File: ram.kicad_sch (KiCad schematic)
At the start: 8 parts, among them U8 HyperRAM

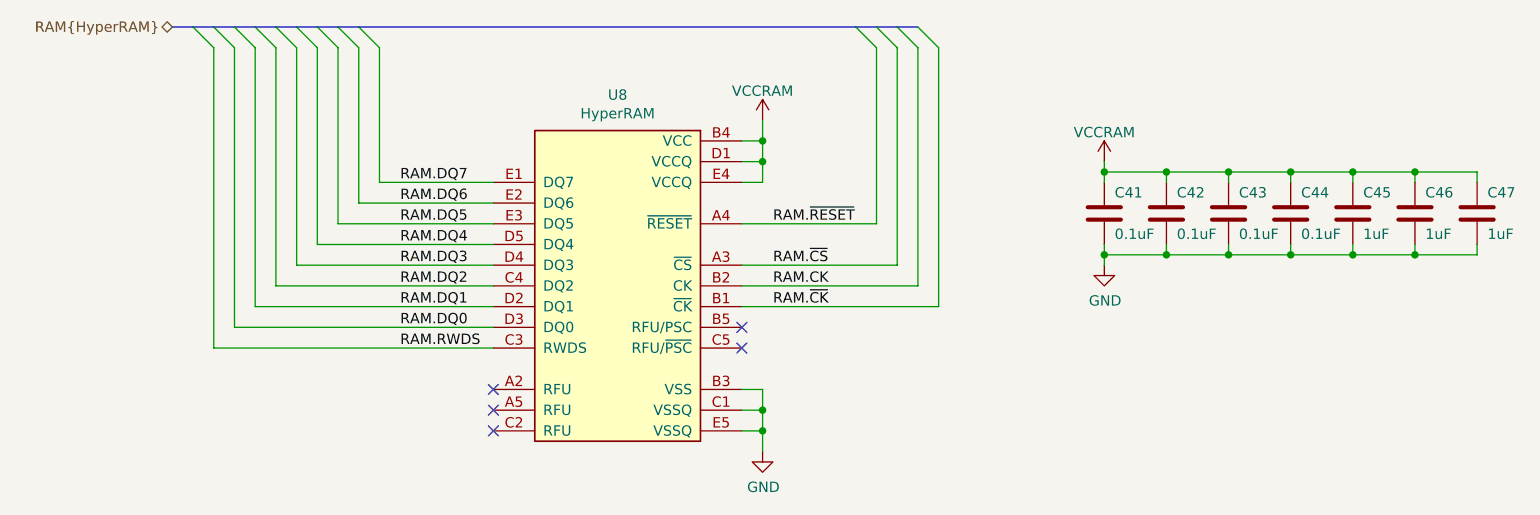
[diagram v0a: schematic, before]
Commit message: Add radio transceiver
Remove Cynthion-specific features
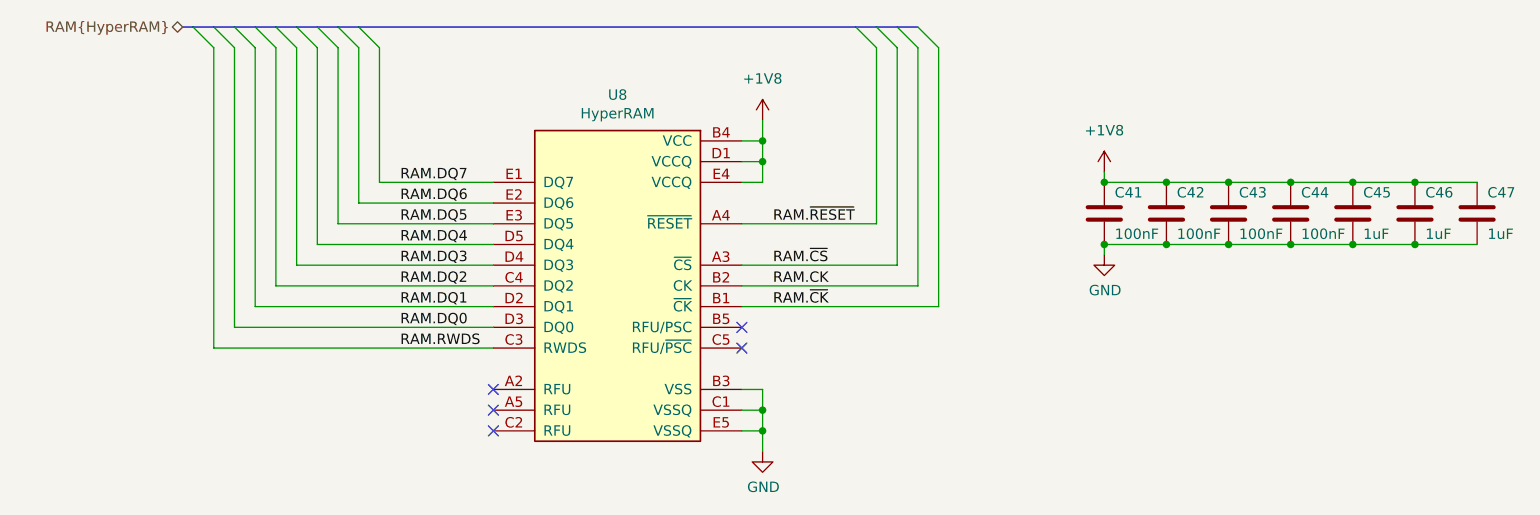
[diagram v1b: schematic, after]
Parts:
- C41, C42, C43, C44: value 0.1uF -> 100nF
- C45, C46, C47: Part Number CL05A105MQ5NNNC -> CL05A105KP5NNNC; Substitution CL05A105KQ5NNNC, CL05A105KP5NNNC, CL05A105KO5NNNC -> any equivalent
- U8: Part Number W956A8MBYA6I -> W956D8MBYA5I TR; Substitution W956A8MBYA5I -> W958D8NWSX4I, W958D8NWSX5I, W958D8NBYA5I, Infineon S27KS064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
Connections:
- net VCCRAM renamed +1V8
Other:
- company: Copyright 2023 Great Scott Gadgets -> ${COPYRIGHT}
- title: URTI Mainboard -> ${TITLE}
